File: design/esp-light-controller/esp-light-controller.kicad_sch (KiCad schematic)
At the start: 6 parts, among them J1 WS2812b, J2 USB_B_Micro, Q1 2N7002

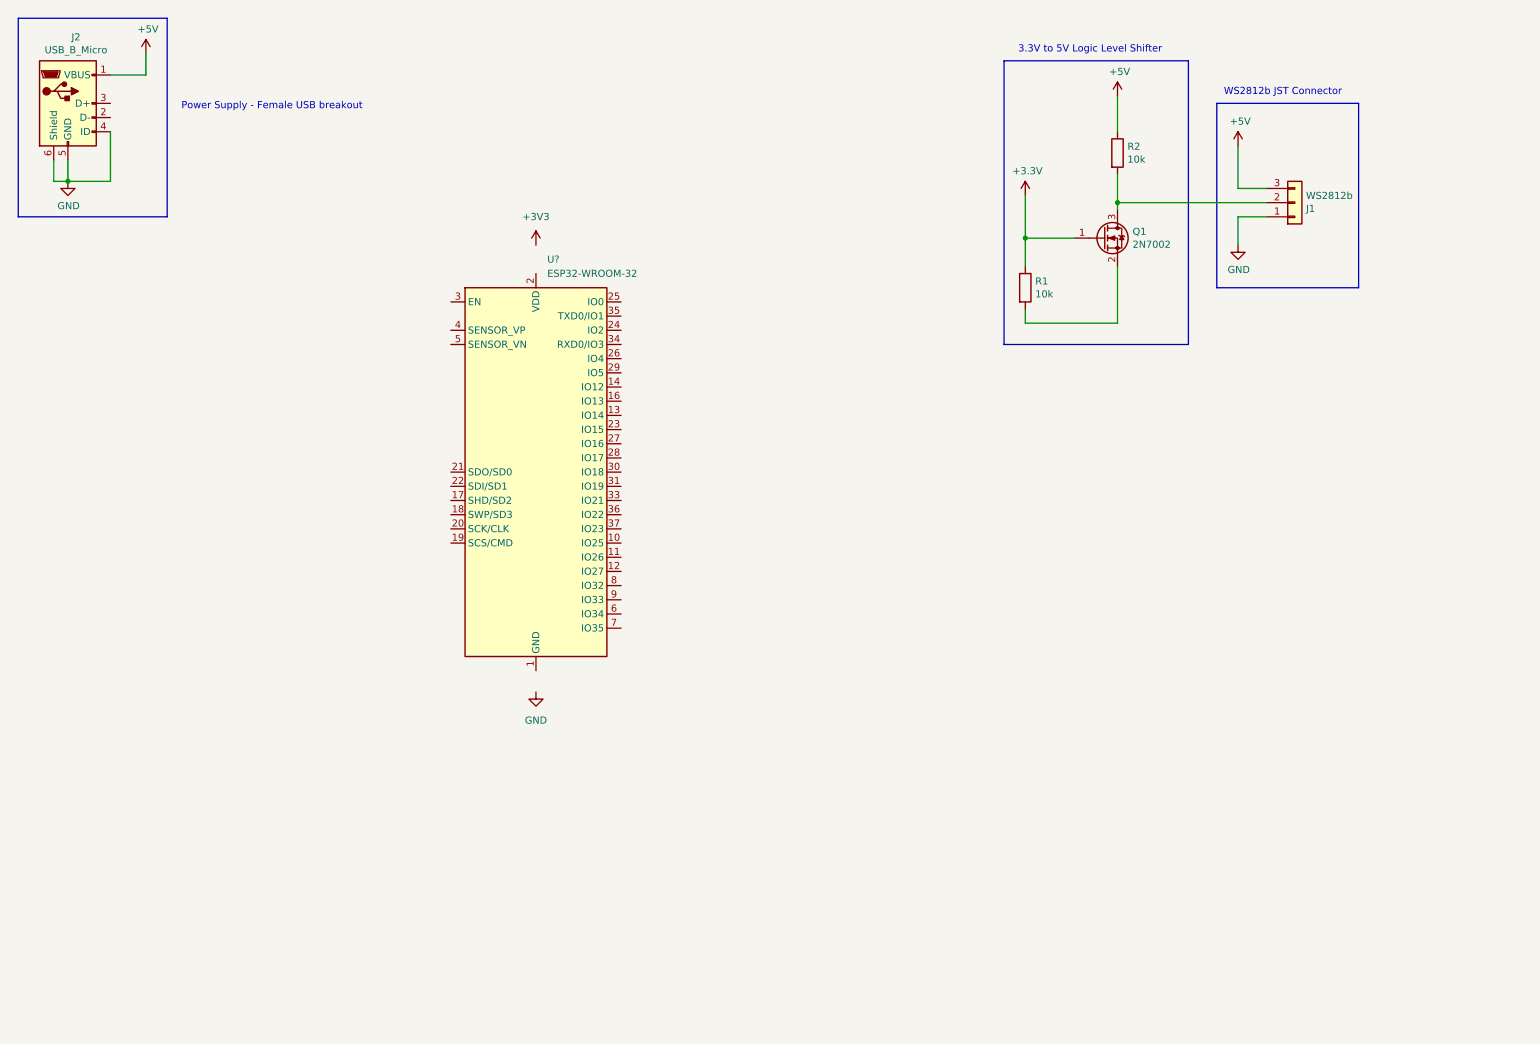
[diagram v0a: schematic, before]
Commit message: ESP32 based design
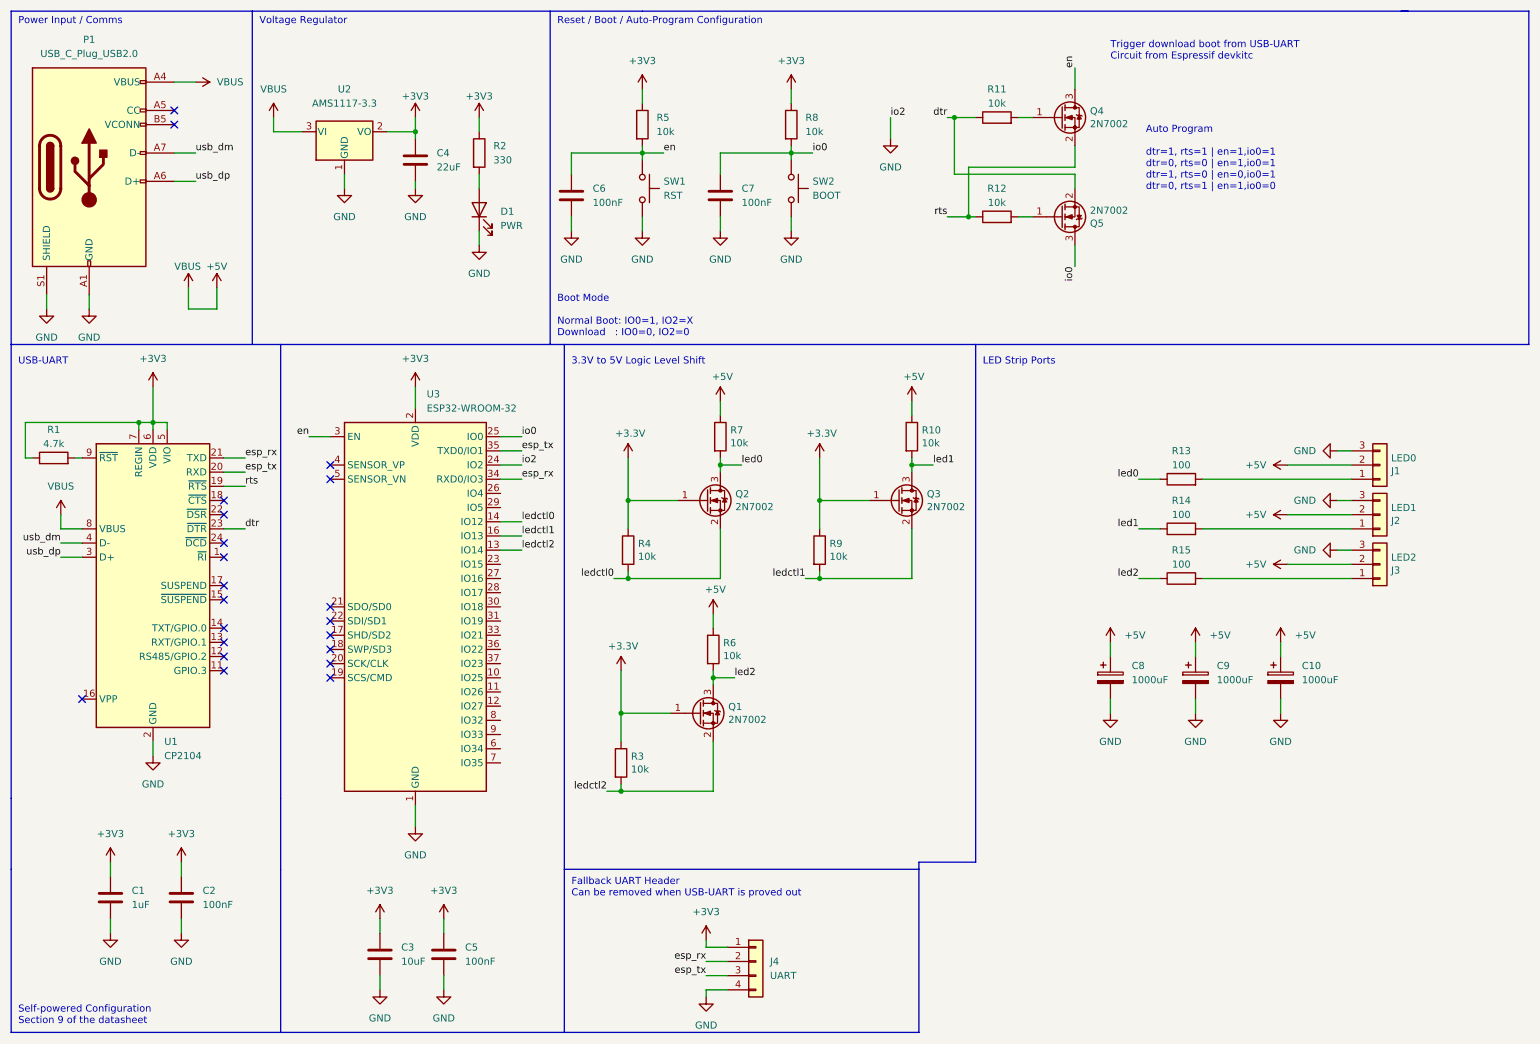
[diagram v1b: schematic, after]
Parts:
- removed J2: USB_B_Micro, digikey-footprints:USB_Micro_B_Female_1050170001, symbol Connector:USB_B_Micro
- added C1: 1uF, Capacitor_SMD:C_0805_2012Metric, symbol Device:C
- added C10, C8, C9: 1000uF, Capacitor_SMD:CP_Elec_8x10, symbol Device:C_Polarized
- added C2, C5, C6, C7: 100nF, Capacitor_SMD:C_0805_2012Metric, symbol Device:C
- added C3: 10uF, Capacitor_SMD:C_0805_2012Metric, symbol Device:C
- added C4: 22uF, Capacitor_Tantalum_SMD:CP_EIA-3216-18_Kemet-A, symbol Device:C
- added D1: PWR, LED_SMD:LED_0805_2012Metric, symbol Device:LED
- added J2: LED1, Connector_PinHeader_2.54mm:PinHeader_1x03_P2.54mm_Vertical, symbol Connector_Generic:Conn_01x03
- added J3: LED2, Connector_PinHeader_2.54mm:PinHeader_1x03_P2.54mm_Vertical, symbol Connector_Generic:Conn_01x03
- added J4: UART, Connector_PinHeader_2.54mm:PinHeader_1x04_P2.54mm_Vertical, symbol Connector_Generic:Conn_01x04
- added P1: USB_C_Plug_USB2.0, ki-usb-connectors:MOLEX_105450-0101, symbol Connector:USB_C_Plug_USB2.0
- added Q1, Q3, Q4, Q5: 2N7002, Package_TO_SOT_SMD:SOT-23, symbol Transistor_FET:2N7002
- added R1: 4.7k, Resistor_SMD:R_0805_2012Metric, symbol Device:R
- added R10, R11, R12, R3, R5, R6, R8, R9: 10k, Resistor_SMD:R_0805_2012Metric, symbol Device:R
- added R13, R14, R15: 100, Resistor_SMD:R_0805_2012Metric, symbol Device:R
- added R2: 330, Resistor_SMD:R_0805_2012Metric, symbol Device:R
- added SW1: RST, tactile_switches:TS-1088-AR02016, symbol Switch:SW_Push
- added SW2: BOOT, tactile_switches:TS-1088-AR02016, symbol Switch:SW_Push
- added U1: CP2104, Package_DFN_QFN:QFN-24-1EP_4x4mm_P0.5mm_EP2.6x2.6mm, symbol Interface_USB:CP2104
- added U2: AMS1117-3.3, Package_TO_SOT_SMD:SOT-223-3_TabPin2, symbol Regulator_Linear:AMS1117-3.3
- J1: value WS2812b -> LED0; footprint Connector_JST:JST_XH_S3B-XH-A_1x03_P2.50mm_Horizontal -> Connector_PinHeader_2.54mm:PinHeader_1x03_P2.54mm_Vertical
- Q2: renamed from Q1; LCSC (none) -> C8545
- R4: renamed from R1; footprint Resistor_SMD:R_0201_0603Metric -> Resistor_SMD:R_0805_2012Metric; LCSC (none) -> C17414
- R7: renamed from R2; footprint Resistor_SMD:R_0201_0603Metric -> Resistor_SMD:R_0805_2012Metric; LCSC (none) -> C17414
- U3: renamed from U?; LCSC (none) -> C82899
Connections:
- net +3V3: now also U3.2 (VDD), C1.1, C2.1, C3.1, C4.1, C5.1, J4.1 (Pin_1), Q1.1 (G), Q3.1 (G), R1.1, R2.1, R3.1, R5.1, R8.1, R9.1, U1.5 (VIO), U1.6 (VDD), U1.7 (REGIN), U2.2 (VO)
- net +5V: now also J1.2 (Pin_2), C10.1, C8.1, C9.1, J2.2 (Pin_2), J3.2 (Pin_2), P1.A4 (VBUS), P1.A9 (VBUS), P1.B4 (VBUS), P1.B9 (VBUS), R10.1, R6.1, U1.8 (VBUS), U2.3 (VI); no longer J1.3 (Pin_3)
- net GND: now also J1.3 (Pin_3), U3.1 (GND), U3.15 (GND), U3.24 (IO2), U3.38 (GND), U3.39 (GND), C1.2, C10.2, C2.2, C3.2, C4.2, C5.2, C6.2, C7.2, C8.2, C9.2, D1.1 (K), J2.3 (Pin_3), J3.3 (Pin_3), J4.4 (Pin_4), P1.A1 (GND), P1.A12 (GND), P1.B1 (GND), P1.B12 (GND), P1.S1 (SHIELD), SW1.2, SW2.2, U1.2 (GND), U1.25 (GND), U2.1 (GND); no longer J1.1 (Pin_1)
- net led0: now reaches Q2.3 (D), R7.2
- net led0: now also R13.1; no longer J1.2 (Pin_2)
- net ledctl0: now reaches Q2.2 (S), R4.2
- net ledctl0: now also U3.14 (IO12)
- net ledctl2: now reaches U3.13 (IO14)
- net ledctl2: now also Q1.2 (S), R3.2
- net ledctl1: now reaches U3.16 (IO13)
- net ledctl1: now also Q3.2 (S), R9.2
- net io0: now reaches U3.25 (IO0)
- net io0: now also C7.1, Q5.3 (D), R8.2, SW2.1
- net en: now reaches U3.3 (EN)
- net en: now also C6.1, Q4.3 (D), R5.2, SW1.1
- net esp_rx: now reaches U3.34 (RXD0/IO3)
- net esp_rx: now also J4.2 (Pin_2), U1.21 (TXD)
- net esp_tx: now reaches U3.35 (TXD0/IO1)
- net esp_tx: now also J4.3 (Pin_3), U1.20 (RXD)
- new net: J1.1 (Pin_1), R13.2
- new net: R1.2, U1.9 (~{RST})
- new net: D1.2 (A), R2.2
- new net: J2.1 (Pin_1), R14.2
- new net: Q4.1 (G), R11.2
- new net: Q5.1 (G), R12.2
- new net: J3.1 (Pin_1), R15.2
- new net dtr: Q5.2 (S), R11.1, U1.23 (~{DTR})
- new net led1: Q3.3 (D), R10.2, R14.1
- new net led2: Q1.3 (D), R15.1, R6.2
- new net rts: Q4.2 (S), R12.1, U1.19 (~{RTS})
- new net usb_dm: P1.A7 (D-), U1.4 (D-)
- new net usb_dp: P1.A6 (D+), U1.3 (D+)
- no-connect marks 0 -> 21
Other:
- note added: "3.3V to 5V Logic Level Shift"
- note added: "Auto Program dtr=1, rts=1 | en=1,io0=1 dtr=0, rts=0 | en=1,io0=1 dtr=1, rts=0 | en=0,io0=1 dtr=0, rts=1 | en=1,io0=0"
- note added: "Boot Mode Normal Boot: IO0=1, IO2=X Download : IO0=0, IO2=0"
- note added: "Fallback UART Header Can be removed when USB-UART is proved out"
- note added: "LED Strip Ports"
- note added: "Power Input / Comms"
- note added: "Reset / Boot / Auto-Program Configuration"
- note added: "Self-powered Configuration Section 9 of the datasheet"
- note added: "Trigger download boot from USB-UART Circuit from Espressif devkitc"
- note added: "USB-UART"
- note added: "Voltage Regulator"
- note removed: "3.3V to 5V Logic Level Shifter"
- note removed: "Power Supply - Female USB breakout"
- note removed: "WS2812b JST Connector"
- title: ESP-01 Light Controller -> ESP Light Controller
- moved on the sheet: J1, Q2, R4, R7, U3

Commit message: update pwr led to more available part
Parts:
- D1: LCSC C95814 -> C434432
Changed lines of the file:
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@@
       (effects (font (size 1.27 1.27)) hide)
     )
-    (property "LCSC" "C95814" (id 4) (at 96.52 48.26 90)
+    (property "LCSC" "C434432" (id 4) (at 96.52 48.26 90)
       (effects (font (size 1.27 1.27)) hide)
     )

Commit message: Resolves #38. Select USB-C Connector that works for JLCPCB assembly
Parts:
- P1: footprint ki-usb-connectors:MOLEX_105450-0101 -> USB-C-Connectors:TYPE-C-31-M-04; LCSC C134092 -> C129018
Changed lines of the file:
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@@
     (property "Reference" "P1" (id 0) (at 26.67 17.78 0))
     (property "Value" "USB_C_Plug_USB2.0" (id 1) (at 26.67 20.32 0))
-    (property "Footprint" "ki-usb-connectors:MOLEX_105450-0101" (id 2) (at 30.48 40.64 0)
-      (effects (font (size 1.27 1.27)) hide)
-    )
-    (property "Datasheet" "https://www.usb.org/sites/default/files/documents/usb_type-c.zip" (id 3) (at 30.48 40.64 0)
-      (effects (font (size 1.27 1.27)) hide)
-    )
-    (property "LCSC" "C134092" (id 4) (at 26.67 40.64 0)
+    (property "Footprint" "USB-C-Connectors:TYPE-C-31-M-04" (id 2) (at 30.48 40.64 0)
+      (effects (font (size 1.27 1.27)) hide)
+    )
+    (property "Datasheet" "https://datasheet.lcsc.com/lcsc/2108131530_Korean-Hroparts-Elec-TYPE-C-31-M-04_C129018.pdf" (id 3) (at 30.48 40.64 0)
+      (effects (font (size 1.27 1.27)) hide)
+    )
+    (property "LCSC" "C129018" (id 4) (at 26.67 40.64 0)
       (effects (font (size 1.27 1.27)) hide)
     )
@@
     )
     (path "/84625814-3c34-4997-9c1c-566a30048a0f"
-      (reference "P1") (unit 1) (value "USB_C_Plug_USB2.0") (footprint "ki-usb-connectors:MOLEX_105450-0101")
+      (reference "P1") (unit 1) (value "USB_C_Plug_USB2.0") (footprint "USB-C-Connectors:TYPE-C-31-M-04")
     )
     (path "/a86e62ef-3572-4970-9a6e-9e16a75389a3"

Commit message: Resolves #39, #40, #43. Rev D.
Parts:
- added Q6: 2N7002, Package_TO_SOT_SMD:SOT-23, symbol Transistor_FET:2N7002
- added R16, R17: 10k, Resistor_SMD:R_0805_2012Metric, symbol Device:R
- added U4: DS18B20Z, Package_SO:SOIC-8_3.9x4.9mm_P1.27mm, symbol Sensor_Temperature:DS18B20Z
- J4: value UART -> PWM_FAN
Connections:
- net +3V3: now also Q6.1 (G), R16.1, U4.3 (VDD); no longer J4.1 (Pin_1)
- net +5V: now also J4.3 (Pin_3), R17.1
- net GND: now also U3.14 (IO12), U4.5 (GND)
- net esp_rx: no longer J4.2 (Pin_2)
- net esp_tx: no longer J4.3 (Pin_3)
- net ledctl0: now also U3.16 (IO13); no longer U3.14 (IO12)
- net ledctl1: now also U3.13 (IO14); no longer U3.16 (IO13)
- net ledctl2: now also U3.23 (IO15); no longer U3.13 (IO14)
- net fanctl: now reaches U3.27 (IO16)
- net fanctl: now also Q6.2 (S), R16.2
- net tach: now reaches U3.28 (IO17)
- net tach: now also J4.2 (Pin_2)
- net at U3.30 (IO18): now also U4.4 (DQ)
- new net fan: J4.1 (Pin_1), Q6.3 (D), R17.2
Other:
- note added: "Fan / Temperature Control"
- note removed: "Fallback UART Header Can be removed when USB-UART is proved out"
- moved on the sheet: Q1, R3, R6
